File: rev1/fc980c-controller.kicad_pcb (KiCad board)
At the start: 2 copper layers, 82.2 x 35.5 mm, 36 parts, among them J1 SWD, J2 USB, J3 KEYBOARD, SW1 BOOT0, U1 XC6206P332MR, U2 STM32F401CBUx, U3 USBLC6-2SC6, U4 M24C64-RMN6TP, U5 PCA9306DC, Y1 8MHz Cl 20pF

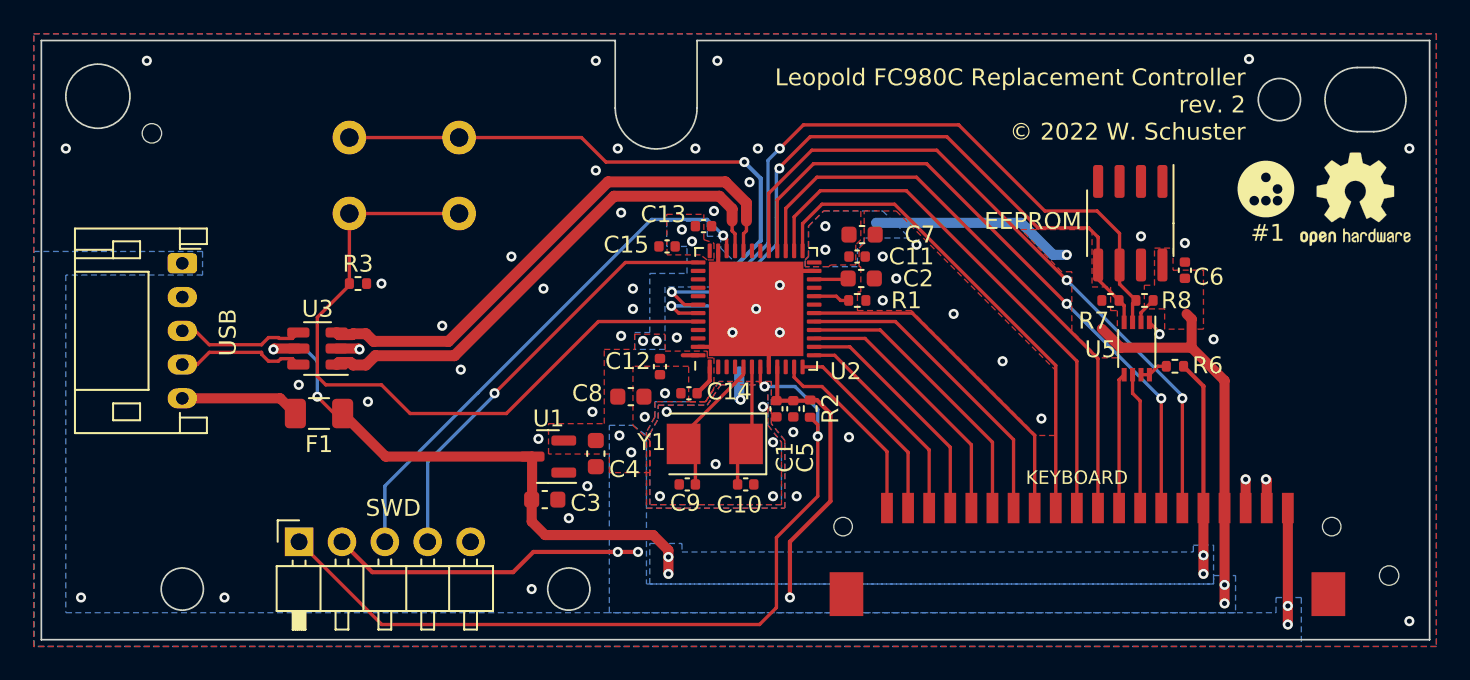
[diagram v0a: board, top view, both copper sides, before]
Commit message: rev1: Revert rev2 changes
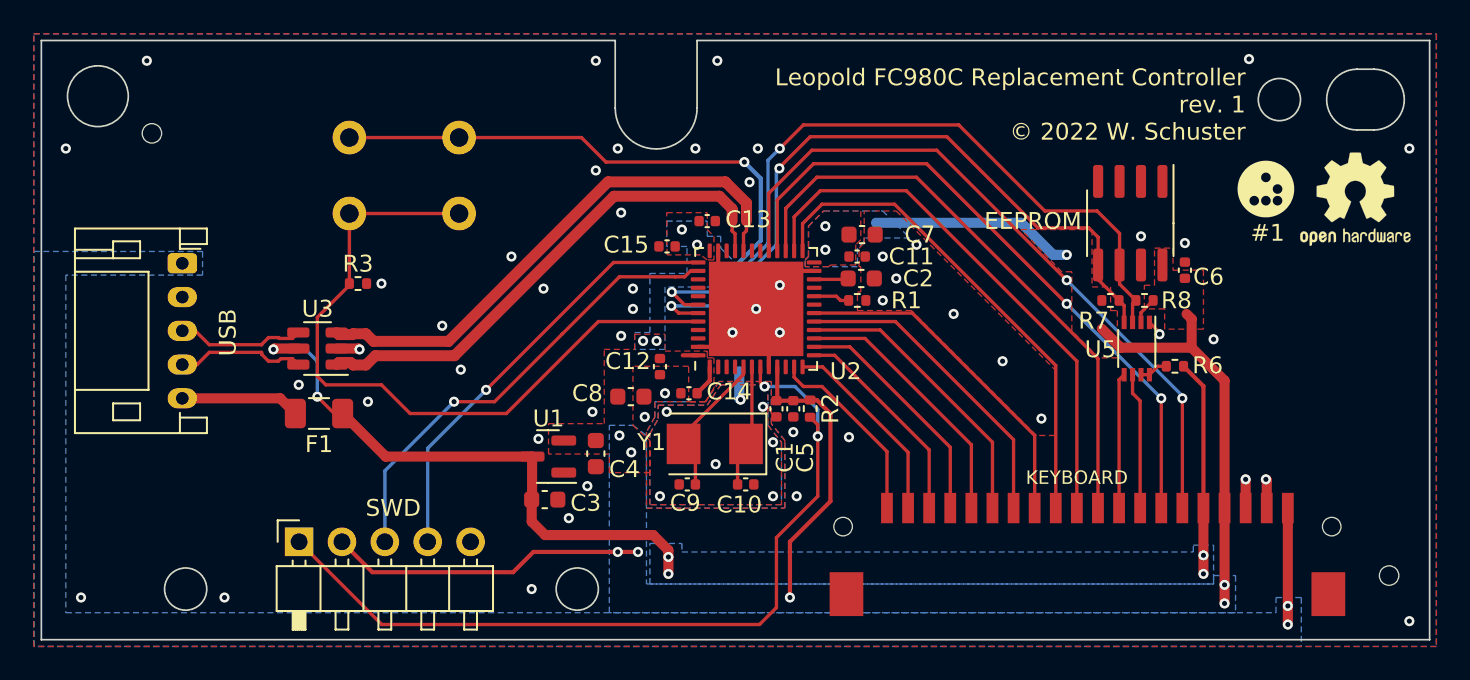
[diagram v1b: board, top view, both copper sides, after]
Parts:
- moved C13 0.37 mm to (114.2, 46.2)
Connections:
- U2 pad 34: SWDIO -> unconnected-(U2-Pad34)
- U2 pad 38: unconnected-(U2-Pad38) -> SWDIO
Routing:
- net SWDIO: track 31.3 -> 27.7 mm
- net GND: vias 62 -> 60
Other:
- outline, holes or cut-outs redrawn
- board text added: "Leopold FC980C Replacement Controller rev. 1 © 2022 W. Schuster"
- board text removed: "Leopold FC980C Replacement Controller rev. 2 © 2022 W. Schuster"
